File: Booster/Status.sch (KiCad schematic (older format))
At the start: 0 parts

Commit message: Added reversing support. Working on status output.
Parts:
- added D?: Status_LED, symbol LED_Dual_ACA
- added U?: 74HC04, symbol 74HC04
- added U?: 74LS08, symbol 74LS08
- added U?: 74LS86, symbol 74LS86
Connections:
- net labels added: DCC_ENABLE, DRIVER_ENABLE, ~OVERCURRENT
- wire segments 0 -> 10
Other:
- note added: "LED status:\nOff: Master switch off\nGreen: DCC signal present and output\nYellow: DCC disabled (from central)\nRed: Overcurrent\nRED"
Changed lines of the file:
@@
 $Descr A4 11693 8268
 encoding utf-8
-Sheet 6 6
+Sheet 6 7
 Title ""
 Date ""
@@
 Comment4 ""
 $EndDescr
+Text HLabel 1950 3600 0    60   Input ~ 0
+DCC_ENABLE
+Text HLabel 2100 4400 0    60   Input ~ 0
+~OVERCURRENT
+Text HLabel 8250 3700 2    60   Output ~ 0
+DRIVER_ENABLE
+Text Notes 3650 7050 0    60   ~ 0
+LED status:\nOff: Master switch off\nGreen: DCC signal present and output\nYellow: DCC disabled (from central)\nRed: Overcurrent\nRED
+$Comp
+L LED_Dual_ACA D?
+U 1 1 5A08D8B5
+P 6500 2700
+F 0 "D?" H 6500 2925 50  0000 C CNN
+F 1 "Status_LED" H 6500 2450 50  0000 C CNN
+F 2 "" H 6500 2700 50  0000 C CNN
+F 3 "" H 6500 2700 50  0000 C CNN
+	1    6500 2700
+	0    1    1    0
+$EndComp
+$Comp
+L 74HC04 U?
+U 1 1 5A08DC01
+P 3150 4400
+F 0 "U?" H 3300 4500 50  0000 C CNN
+F 1 "74HC04" H 3350 4300 50  0000 C CNN
+F 2 "" H 3150 4400 50  0000 C CNN
+F 3 "" H 3150 4400 50  0000 C CNN
+	1    3150 4400
+	1    0    0    -1
+$EndComp
+$Comp
+L 74LS08 U?
+U 1 1 5A08E1A2
+P 5450 3700
+F 0 "U?" H 5450 3750 50  0000 C CNN
+F 1 "74LS08" H 5450 3650 50  0000 C CNN
+F 2 "" H 5450 3700 50  0000 C CNN
+F 3 "" H 5450 3700 50  0000 C CNN
+	1    5450 3700
+	1    0    0    -1
+$EndComp
+$Comp
+L 74LS86 U?
+U 1 1 5A08E4A0
+P 5200 5300
+F 0 "U?" H 5250 5350 50  0000 C CNN
+F 1 "74LS86" H 5250 5250 50  0000 C CNN
+F 2 "" H 5200 5300 50  0000 C CNN
+F 3 "" H 5200 5300 50  0000 C CNN
+	1    5200 5300
+	1    0    0    -1
+$EndComp
+Wire Wire Line
+	2100 4400 2700 4400
+Wire Wire Line
+	3600 4400 6900 4400
+Wire Wire Line
+	1950 3600 4850 3600
+Wire Wire Line
+	3850 3800 3850 5200
+Wire Wire Line
+	3850 3800 4850 3800
+Connection ~ 3850 4400
+Wire Wire Line
+	4600 5400 2350 5400
+Wire Wire Line
+	2350 5400 2350 3600
+Connection ~ 2350 3600
+Wire Wire Line
+	5800 5300 6900 5300
+Wire Wire Line
+	6050 3700 8250 3700
+Wire Wire Line
+	3850 5200 4600 5200
 $EndSCHEMATC

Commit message: Added initial logic to the status. Still need to hook up LED, validate, and optimize for fewer gates if possible.
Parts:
- added P?: CONN_01X02, symbol CONN_01X02
- added R?: 10K, symbol R
- added SW?: SW_DIP_x01, symbol SW_DIP_x01
- added U?: 74LS08, symbol 74LS08
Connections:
- net labels added: +5V, GND
- wire segments 10 -> 33
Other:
- moved on the sheet: D?, U?A
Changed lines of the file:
@@
 Comment4 ""
 $EndDescr
-Text HLabel 1950 3600 0    60   Input ~ 0
+Text HLabel 1950 3200 0    60   Input ~ 0
 DCC_ENABLE
 Text HLabel 2100 4400 0    60   Input ~ 0
 ~OVERCURRENT
-Text HLabel 8250 3700 2    60   Output ~ 0
+Text HLabel 10250 3400 2    60   Output ~ 0
 DRIVER_ENABLE
 Text Notes 3650 7050 0    60   ~ 0
@@
 L LED_Dual_ACA D?
 U 1 1 5A08D8B5
-P 6500 2700
-F 0 "D?" H 6500 2925 50  0000 C CNN
-F 1 "Status_LED" H 6500 2450 50  0000 C CNN
-F 2 "" H 6500 2700 50  0000 C CNN
-F 3 "" H 6500 2700 50  0000 C CNN
-	1    6500 2700
-	0    1    1    0
+P 6950 5450
+F 0 "D?" H 6950 5675 50  0000 C CNN
+F 1 "Status_LED" H 6950 5200 50  0000 C CNN
+F 2 "" H 6950 5450 50  0000 C CNN
+F 3 "" H 6950 5450 50  0000 C CNN
+	1    6950 5450
+	-1   0    0    1
 $EndComp
 $Comp
 L 74HC04 U?
 U 1 1 5A08DC01
-P 3150 4400
-F 0 "U?" H 3300 4500 50  0000 C CNN
-F 1 "74HC04" H 3350 4300 50  0000 C CNN
-F 2 "" H 3150 4400 50  0000 C CNN
-F 3 "" H 3150 4400 50  0000 C CNN
-	1    3150 4400
+P 2850 4400
+F 0 "U?" H 3000 4500 50  0000 C CNN
+F 1 "74HC04" H 3050 4300 50  0000 C CNN
+F 2 "" H 2850 4400 50  0000 C CNN
+F 3 "" H 2850 4400 50  0000 C CNN
+	1    2850 4400
 	1    0    0    -1
 $EndComp
@@
 L 74LS08 U?
 U 1 1 5A08E1A2
-P 5450 3700
-F 0 "U?" H 5450 3750 50  0000 C CNN
-F 1 "74LS08" H 5450 3650 50  0000 C CNN
-F 2 "" H 5450 3700 50  0000 C CNN
-F 3 "" H 5450 3700 50  0000 C CNN
-	1    5450 3700
+P 4400 3300
+F 0 "U?" H 4400 3350 50  0000 C CNN
+F 1 "74LS08" H 4400 3250 50  0000 C CNN
+F 2 "" H 4400 3300 50  0000 C CNN
+F 3 "" H 4400 3300 50  0000 C CNN
+	1    4400 3300
 	1    0    0    -1
 $EndComp
@@
 L 74LS86 U?
 U 1 1 5A08E4A0
-P 5200 5300
-F 0 "U?" H 5250 5350 50  0000 C CNN
-F 1 "74LS86" H 5250 5250 50  0000 C CNN
-F 2 "" H 5200 5300 50  0000 C CNN
-F 3 "" H 5200 5300 50  0000 C CNN
-	1    5200 5300
+P 6000 3900
+F 0 "U?" H 6050 3950 50  0000 C CNN
+F 1 "74LS86" H 6050 3850 50  0000 C CNN
+F 2 "" H 6000 3900 50  0000 C CNN
+F 3 "" H 6000 3900 50  0000 C CNN
+	1    6000 3900
 	1    0    0    -1
 $EndComp
 Wire Wire Line
-	2100 4400 2700 4400
+	2100 4400 2400 4400
 Wire Wire Line
-	3600 4400 6900 4400
+	1950 3200 3800 3200
 Wire Wire Line
-	1950 3600 4850 3600
+	3550 3400 3550 4400
 Wire Wire Line
-	3850 3800 3850 5200
+	3550 3400 3800 3400
+Connection ~ 3550 4400
 Wire Wire Line
-	3850 3800 4850 3800
-Connection ~ 3850 4400
+	5000 3300 5250 3300
 Wire Wire Line
-	4600 5400 2350 5400
+	5250 3300 7200 3300
 Wire Wire Line
-	2350 5400 2350 3600
-Connection ~ 2350 3600
+	7200 3300 8250 3300
 Wire Wire Line
-	5800 5300 6900 5300
+	5400 3800 5250 3800
 Wire Wire Line
-	6050 3700 8250 3700
+	5250 3800 5250 3300
+Connection ~ 5250 3300
 Wire Wire Line
-	3850 5200 4600 5200
+	5400 4000 5250 4000
+Wire Wire Line
+	3300 4400 3550 4400
+Wire Wire Line
+	3550 4400 5250 4400
+Wire Wire Line
+	5250 4400 5250 4000
+Wire Wire Line
+	6600 3900 7050 3900
+Wire Wire Line
+	7050 3900 7050 4350
+$Comp
+L 74LS08 U?
+U 1 1 5A093D74
+P 8850 3400
+F 0 "U?" H 8850 3450 50  0000 C CNN
+F 1 "74LS08" H 8850 3350 50  0000 C CNN
+F 2 "" H 8850 3400 50  0000 C CNN
+F 3 "" H 8850 3400 50  0000 C CNN
+	1    8850 3400
+	1    0    0    -1
+$EndComp
+Wire Wire Line
+	10250 3400 9450 3400
+$Comp
+L CONN_01X02 P?
+U 1 1 5A093E16
+P 8750 4200
+F 0 "P?" H 8750 4350 50  0000 C CNN
+F 1 "CONN_01X02" V 8850 4200 50  0000 C CNN
+F 2 "" H 8750 4200 50  0000 C CNN
+F 3 "" H 8750 4200 50  0000 C CNN
+	1    8750 4200
+	1    0    0    -1
+$EndComp
+Wire Wire Line
+	8250 3500 8200 3500
+Wire Wire Line
+	8200 3500 8200 4150
+Wire Wire Line
+	8200 4150 8200 4350
+Wire Wire Line
+	8100 4150 8200 4150
+Wire Wire Line
+	8200 4150 8400 4150
+Wire Wire Line
+	8400 4150 8550 4150
+$Comp
+L R R?
+U 1 1 5A093EA9
+P 7950 4150
+F 0 "R?" V 8030 4150 50  0000 C CNN
+F 1 "10K" V 7950 4150 50  0000 C CNN
+F 2 "" V 7880 4150 50  0001 C CNN
+F 3 "" H 7950 4150 50  0001 C CNN
+	1    7950 4150
+	0    1    1    0
+$EndComp
+Wire Wire Line
+	7800 4150 7550 4150
+Wire Wire Line
+	7550 4150 7550 3900
+$Comp
+L +5V #PWR?
+U 1 1 5A093F5C
+P 7550 3900
+F 0 "#PWR?" H 7550 3750 50  0001 C CNN
+F 1 "+5V" H 7550 4040 50  0000 C CNN
+F 2 "" H 7550 3900 50  0001 C CNN
+F 3 "" H 7550 3900 50  0001 C CNN
+	1    7550 3900
+	1    0    0    -1
+$EndComp
+Wire Wire Line
+	8550 4250 8300 4250
+Wire Wire Line
+	8300 4250 8300 5200
+Wire Wire Line
+	8300 5200 8300 5400
+Connection ~ 8200 4150
+$Comp
+L GND #PWR?
+U 1 1 5A094169
+P 8300 5400
+F 0 "#PWR?" H 8300 5150 50  0001 C CNN
+F 1 "GND" H 8300 5250 50  0000 C CNN
+F 2 "" H 8300 5400 50  0001 C CNN
+F 3 "" H 8300 5400 50  0001 C CNN
+	1    8300 5400
+	1    0    0    -1
+$EndComp
+$Comp
+L SW_DIP_x01 SW?
+U 1 1 5A0941BA
+P 8750 4750
+F 0 "SW?" H 8750 4900 50  0000 C CNN
+F 1 "SW_DIP_x01" H 8750 4600 50  0000 C CNN
+F 2 "" H 8750 4750 50  0001 C CNN
+F 3 "" H 8750 4750 50  0001 C CNN
+	1    8750 4750
+	0    1    1    0
+$EndComp
+Wire Wire Line
+	8300 5200 8750 5200
+Wire Wire Line
+	8750 5200 8750 5050
+Connection ~ 8300 5200
+Wire Wire Line
+	8750 4450 8400 4450
+Wire Wire Line
+	8400 4450 8400 4150
+Connection ~ 8400 4150
+Wire Wire Line
+	8200 4350 7400 4350
+Wire Wire Line
+	7200 3300 7200 4350
+Connection ~ 7200 3300
 $EndSCHEMATC

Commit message: Getting close to feature complete for a single channel.
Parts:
- removed SW?: SW_DIP_x01, symbol SW_DIP_x01
- removed U?: 74HC04, symbol 74HC04
- removed U?: 74LS86, symbol 74LS86
- added J?: StatusLED, symbol Conn_01x03
- added P?: ~DRIVER_ENABLE_OUT, symbol CONN_01X02
- added P?: MSTR_SW_OUT, symbol CONN_01X02
- added P?: ~OVERCURRENT_OUT, symbol CONN_01X02
- added P?: ~DRIVER_ENABLE_OUT_OP, symbol CONN_01X02
- added P?: ~MSTR_SW_OUT_OP, symbol CONN_01X02
- added P?: ~OVERCURRENT_OUT_OP, symbol CONN_01X02
- added Q? (x3): BC327, TO_SOT_Packages_THT:TO-92_Molded_Narrow, symbol BC327
- added R? (x3): 1K, symbol R
- added R? (x7): R, symbol R
- added R? (x2): 10K, symbol R
- added SW?: MSTR_SW_BYPASS, symbol SW_SPST
- added U?: 74HC04, symbol 74HC04
- added U? (x3): PC817, Housings_DIP:DIP-4_W7.62mm, symbol PC817
- P?: value CONN_01X02 -> MSTR_SW
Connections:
- net labels added: STATUS_GREEN_LED, STATUS_RED_LED
- wire segments 33 -> 108
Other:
- moved on the sheet: D?, P?, R?, U?A

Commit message: Added meassurement tabs and other general "finalizing touches"
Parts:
- removed SW?: MSTR_SW_BYPASS, symbol SW_SPST
- removed U?: 74HC04, symbol 74HC04
- added SW?: SW_SPST_x02, symbol SW_SPST_x02
- added U?: 74LS86, symbol 74LS86
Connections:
- wire segments 108 -> 109
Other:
- note added: "XOR used as NOT"
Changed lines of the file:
@@
 $Comp
 L 74LS08 U?
-U 1 1 5A093D74
+U 2 1 5A093D74
 P 8500 2150
 F 0 "U?" H 8500 2200 50  0000 C CNN
@@
 F 2 "" H 8500 2150 50  0000 C CNN
 F 3 "" H 8500 2150 50  0000 C CNN
-	1    8500 2150
+	2    8500 2150
 	1    0    0    -1
 $EndComp
@@
 $EndComp
 $Comp
-L 74HC04 U?
-U 1 1 5A0BE78E
-P 3250 3300
-F 0 "U?" H 3400 3400 50  0000 C CNN
-F 1 "74HC04" H 3450 3200 50  0000 C CNN
-F 2 "" H 3250 3300 50  0000 C CNN
-F 3 "" H 3250 3300 50  0000 C CNN
-	1    3250 3300
-	0    1    1    0
-$EndComp
-$Comp
 L R R?
 U 1 1 5A0BE87C
@@
 $EndComp
 $Comp
-L SW_SPST SW?
-U 1 1 5A0D34BB
-P 8100 3700
-F 0 "SW?" H 8100 3825 50  0000 C CNN
-F 1 "MSTR_SW_BYPASS" H 8100 3600 50  0000 C CNN
-F 2 "" H 8100 3700 50  0001 C CNN
-F 3 "" H 8100 3700 50  0001 C CNN
-	1    8100 3700
-	0    -1   -1   0
-$EndComp
-$Comp
 L R R?
 U 1 1 5A0DFB8A
@@
 Wire Wire Line
 	3200 2050 7900 2050
-Wire Wire Line
-	3250 2050 3250 2850
 Connection ~ 3250 2050
 Wire Wire Line
@@
 	3000 4700 5550 4700
 Wire Wire Line
-	3250 3750 3250 4350
-Wire Wire Line
-	3250 4350 3500 4350
+	3350 4050 3350 4350
+Wire Wire Line
+	3350 4350 3500 4350
 Wire Wire Line
 	3800 4350 4000 4350
@@
 	1    0    0    -1
 $EndComp
+$Comp
+L SW_SPST_x02 SW?
+U 1 1 5A0F535E
+P 8100 3700
+F 0 "SW?" H 8100 3825 50  0000 C CNN
+F 1 "SW_SPST_x02" H 8100 3600 50  0000 C CNN
+F 2 "" H 8100 3700 50  0001 C CNN
+F 3 "" H 8100 3700 50  0001 C CNN
+	1    8100 3700
+	0    1    1    0
+$EndComp
+$Comp
+L 74LS86 U?
+U 3 1 5A0F5EBC
+P 3350 3450
+F 0 "U?" H 3400 3500 50  0000 C CNN
+F 1 "74LS86" H 3400 3400 50  0000 C CNN
+F 2 "" H 3350 3450 50  0001 C CNN
+F 3 "" H 3350 3450 50  0001 C CNN
+	3    3350 3450
+	0    1    1    0
+$EndComp
+Wire Wire Line
+	3250 2850 3250 2050
+Wire Wire Line
+	3450 2850 3450 2600
+$Comp
+L +5V #PWR?
+U 1 1 5A0F6209
+P 3450 2600
+F 0 "#PWR?" H 3450 2450 50  0001 C CNN
+F 1 "+5V" H 3450 2740 50  0000 C CNN
+F 2 "" H 3450 2600 50  0001 C CNN
+F 3 "" H 3450 2600 50  0001 C CNN
+	1    3450 2600
+	1    0    0    -1
+$EndComp
+Text Notes 3650 3250 0    60   ~ 0
+XOR used as NOT
 $EndSCHEMATC

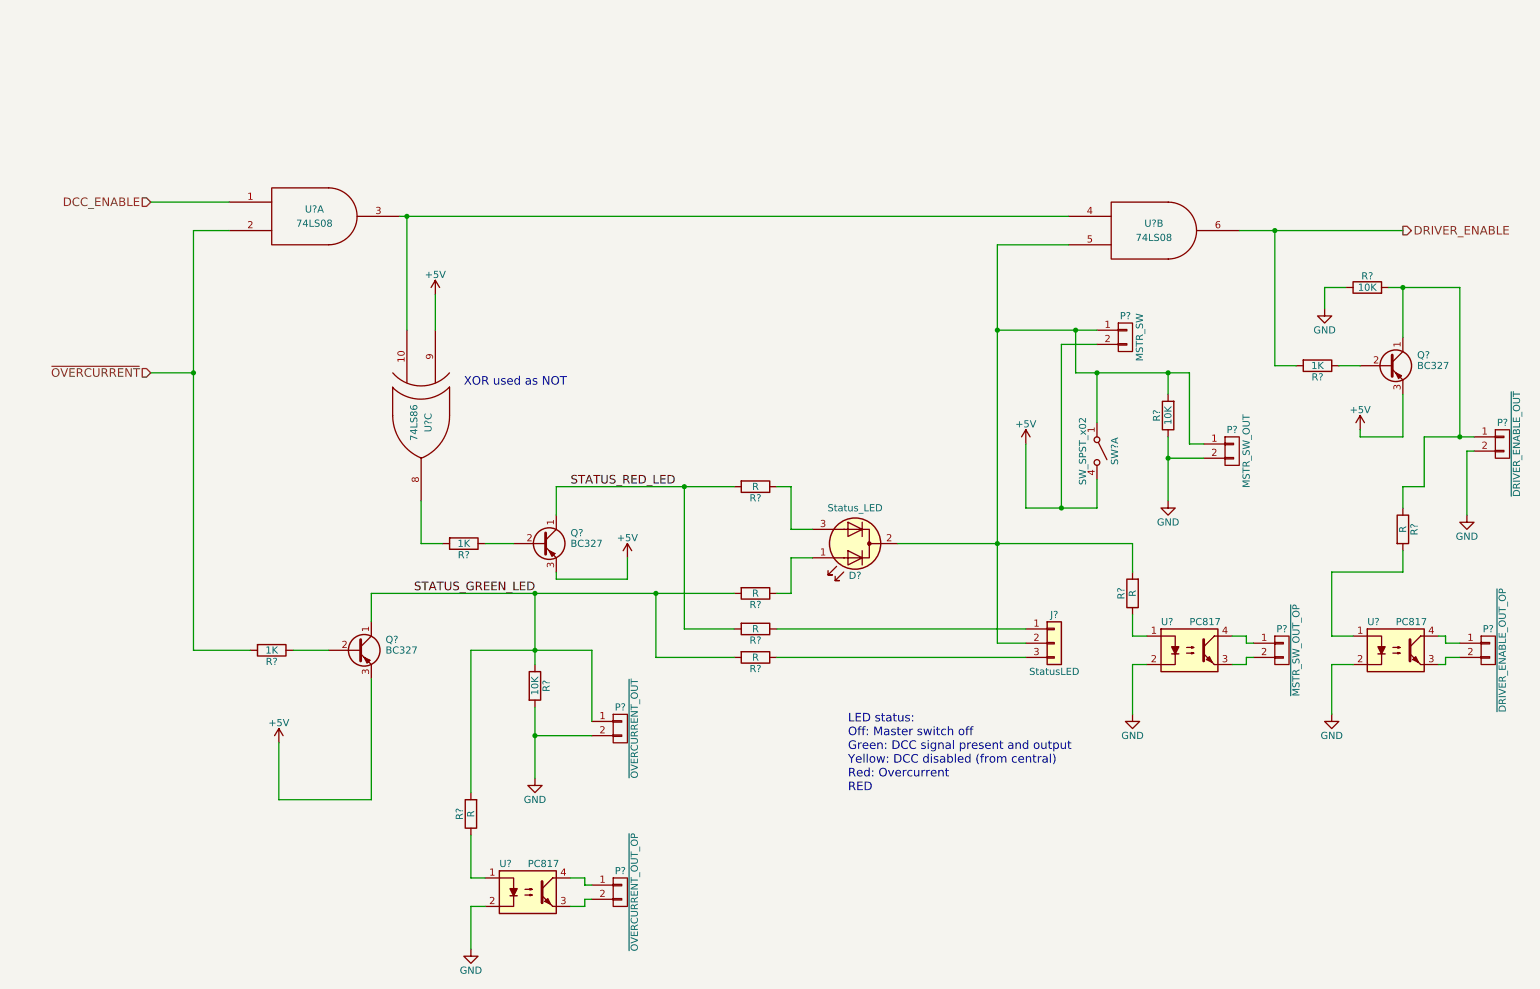
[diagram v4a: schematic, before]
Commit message: Reference voltage of reverser is now the 1V after the resistor dropper. This allows running one wire less to the sensor unit, at the cost of the photo resistor only working off 1V.
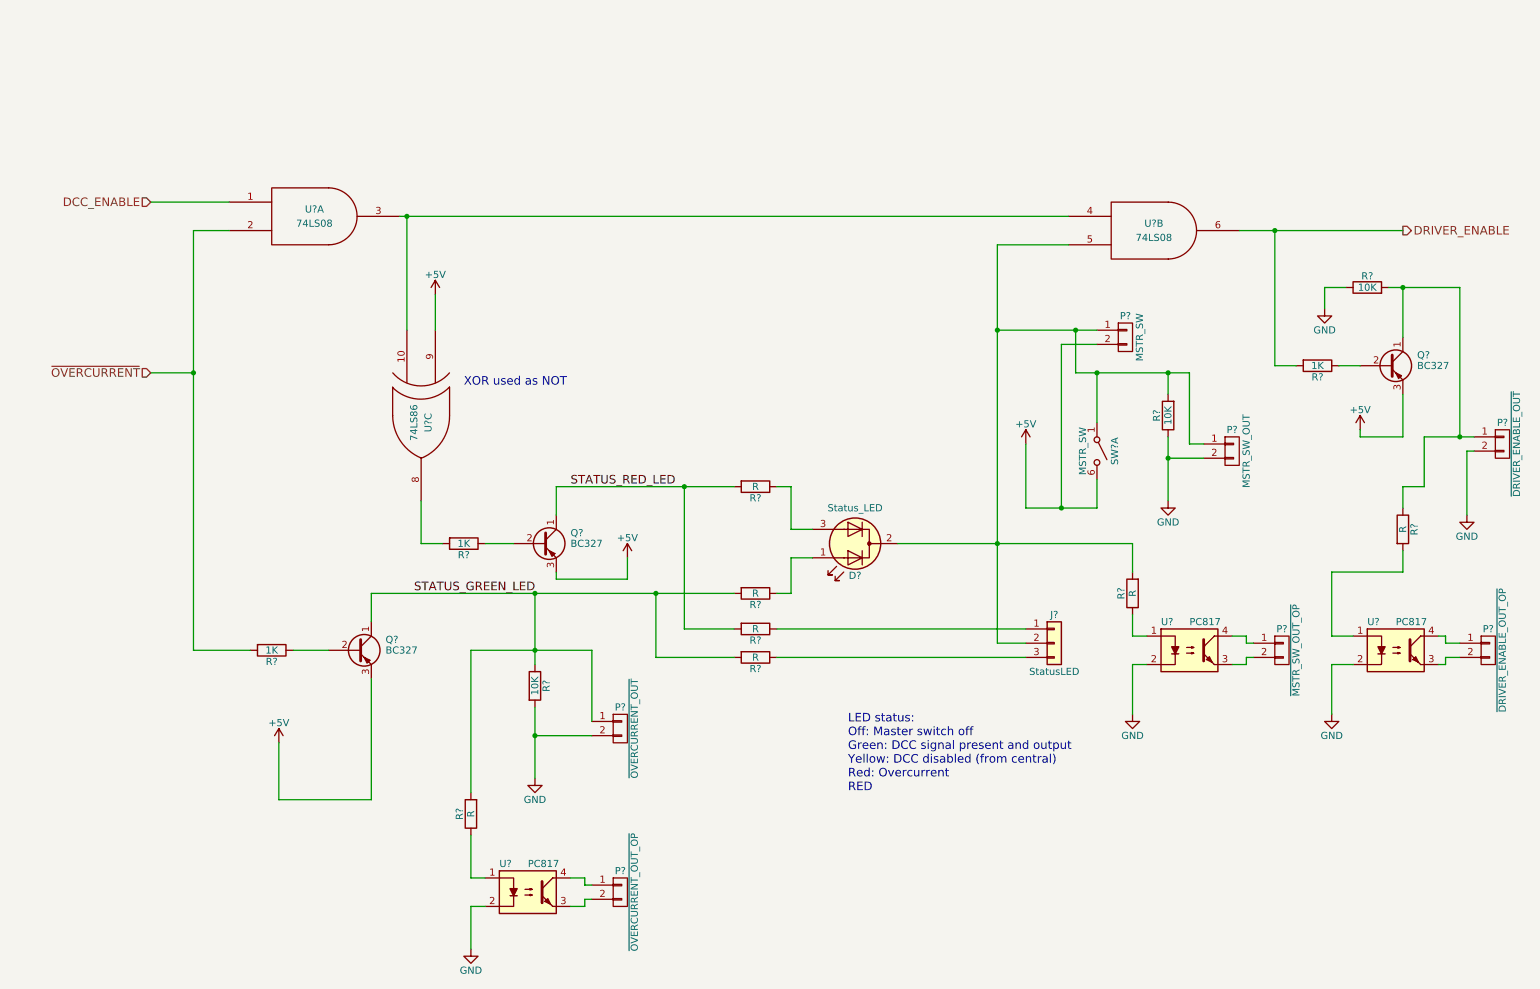
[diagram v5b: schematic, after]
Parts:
- removed SW?: SW_SPST_x02, symbol SW_SPST_x02
- added SW?: MSTR_SW, symbol SW_SPST_x03
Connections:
- net +5V: now also SW?.6 (B)
- net at D?.2 (K), J?.2 (Pin_2), P?.1 (P1)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: now also SW?.1 (A)
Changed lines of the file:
@@
 	1450 1950 2000 1950
 Wire Wire Line
-	1750 2150 1750 5100
+	1750 2150 1750 3150
+Wire Wire Line
+	1750 3150 1750 5100
 Wire Wire Line
 	1750 2150 2000 2150
 Wire Wire Line
-	3200 2050 7900 2050
+	3200 2050 3250 2050
+Wire Wire Line
+	3250 2050 7900 2050
 Connection ~ 3250 2050
 Wire Wire Line
-	9100 2150 10250 2150
+	9100 2150 9350 2150
+Wire Wire Line
+	9350 2150 10250 2150
 Wire Wire Line
 	7400 2250 7900 2250
 Wire Wire Line
-	7400 2250 7400 5050
+	7400 2250 7400 2850
+Wire Wire Line
+	7400 2850 7400 4350
+Wire Wire Line
+	7400 4350 7400 5050
 Wire Wire Line
 	7600 4100 7600 3650
@@
 Connection ~ 7400 2850
 Wire Wire Line
-	7600 4100 8100 4100
+	7600 4100 7850 4100
+Wire Wire Line
+	7850 4100 8100 4100
 Wire Wire Line
 	8100 4100 8100 3900
 Wire Wire Line
-	7950 3150 8750 3150
+	7950 3150 8100 3150
+Wire Wire Line
+	8100 3150 8600 3150
+Wire Wire Line
+	8600 3150 8750 3150
 Wire Wire Line
 	7950 3150 7950 2850
@@
 	3000 4900 3000 4700
 Wire Wire Line
-	3000 4700 5550 4700
+	3000 4700 4150 4700
+Wire Wire Line
+	4150 4700 5000 4700
+Wire Wire Line
+	5000 4700 5550 4700
 Wire Wire Line
 	3350 4050 3350 4350
@@
 	4300 4150 4300 3950
 Wire Wire Line
-	4300 3950 5550 3950
+	4300 3950 5200 3950
+Wire Wire Line
+	5200 3950 5550 3950
 Wire Wire Line
 	6100 4250 5950 4250
@@
 Connection ~ 5000 4700
 Wire Wire Line
-	6700 4350 8350 4350
+	6700 4350 7400 4350
+Wire Wire Line
+	7400 4350 8350 4350
 Wire Wire Line
 	7400 5050 7600 5050
@@
 	7850 2950 7850 4100
 Wire Wire Line
-	7400 2850 8100 2850
+	7400 2850 7950 2850
+Wire Wire Line
+	7950 2850 8100 2850
 Connection ~ 7850 4100
 Wire Wire Line
@@
 	10250 2900 10250 2550
 Wire Wire Line
-	10150 2550 10650 2550
+	10150 2550 10250 2550
+Wire Wire Line
+	10250 2550 10650 2550
 Wire Wire Line
 	10650 2550 10650 3600
 Wire Wire Line
-	10400 3600 10750 3600
+	10400 3600 10650 3600
+Wire Wire Line
+	10650 3600 10750 3600
 Wire Wire Line
 	10250 3600 9950 3600
@@
 	9700 2550 9700 2700
 Wire Wire Line
-	4150 4700 4150 5200
+	4150 4700 4150 5100
+Wire Wire Line
+	4150 5100 4150 5200
 Connection ~ 4150 4700
 Wire Wire Line
-	4150 5500 4150 6000
-Wire Wire Line
-	8600 3600 8600 4050
+	4150 5500 4150 5700
+Wire Wire Line
+	4150 5700 4150 6000
+Wire Wire Line
+	8600 3600 8600 3750
+Wire Wire Line
+	8600 3750 8600 4050
 Wire Wire Line
 	8600 3150 8600 3300
@@
 	4550 5100 4550 5600
 Wire Wire Line
-	3700 5100 4550 5100
+	3700 5100 4150 5100
+Wire Wire Line
+	4150 5100 4550 5100
 Connection ~ 4150 5100
 Wire Wire Line
@@
 $EndComp
 $Comp
-L SW_SPST_x02 SW?
-U 1 1 5A0F535E
-P 8100 3700
-F 0 "SW?" H 8100 3825 50  0000 C CNN
-F 1 "SW_SPST_x02" H 8100 3600 50  0000 C CNN
-F 2 "" H 8100 3700 50  0001 C CNN
-F 3 "" H 8100 3700 50  0001 C CNN
-	1    8100 3700
-	0    1    1    0
-$EndComp
-$Comp
 L 74LS86 U?
 U 3 1 5A0F5EBC
@@
 Text Notes 3650 3250 0    60   ~ 0
 XOR used as NOT
+$Comp
+L SW_SPST_x03 SW?
+U 1 1 5A1062CE
+P 8100 3700
+F 0 "SW?" H 8100 3825 50  0000 C CNN
+F 1 "MSTR_SW" H 8100 3600 50  0000 C CNN
+F 2 "" H 8100 3700 50  0001 C CNN
+F 3 "" H 8100 3700 50  0001 C CNN
+	1    8100 3700
+	0    1    1    0
+$EndComp
 $EndSCHEMATC
